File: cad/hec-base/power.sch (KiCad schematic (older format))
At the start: 45 parts

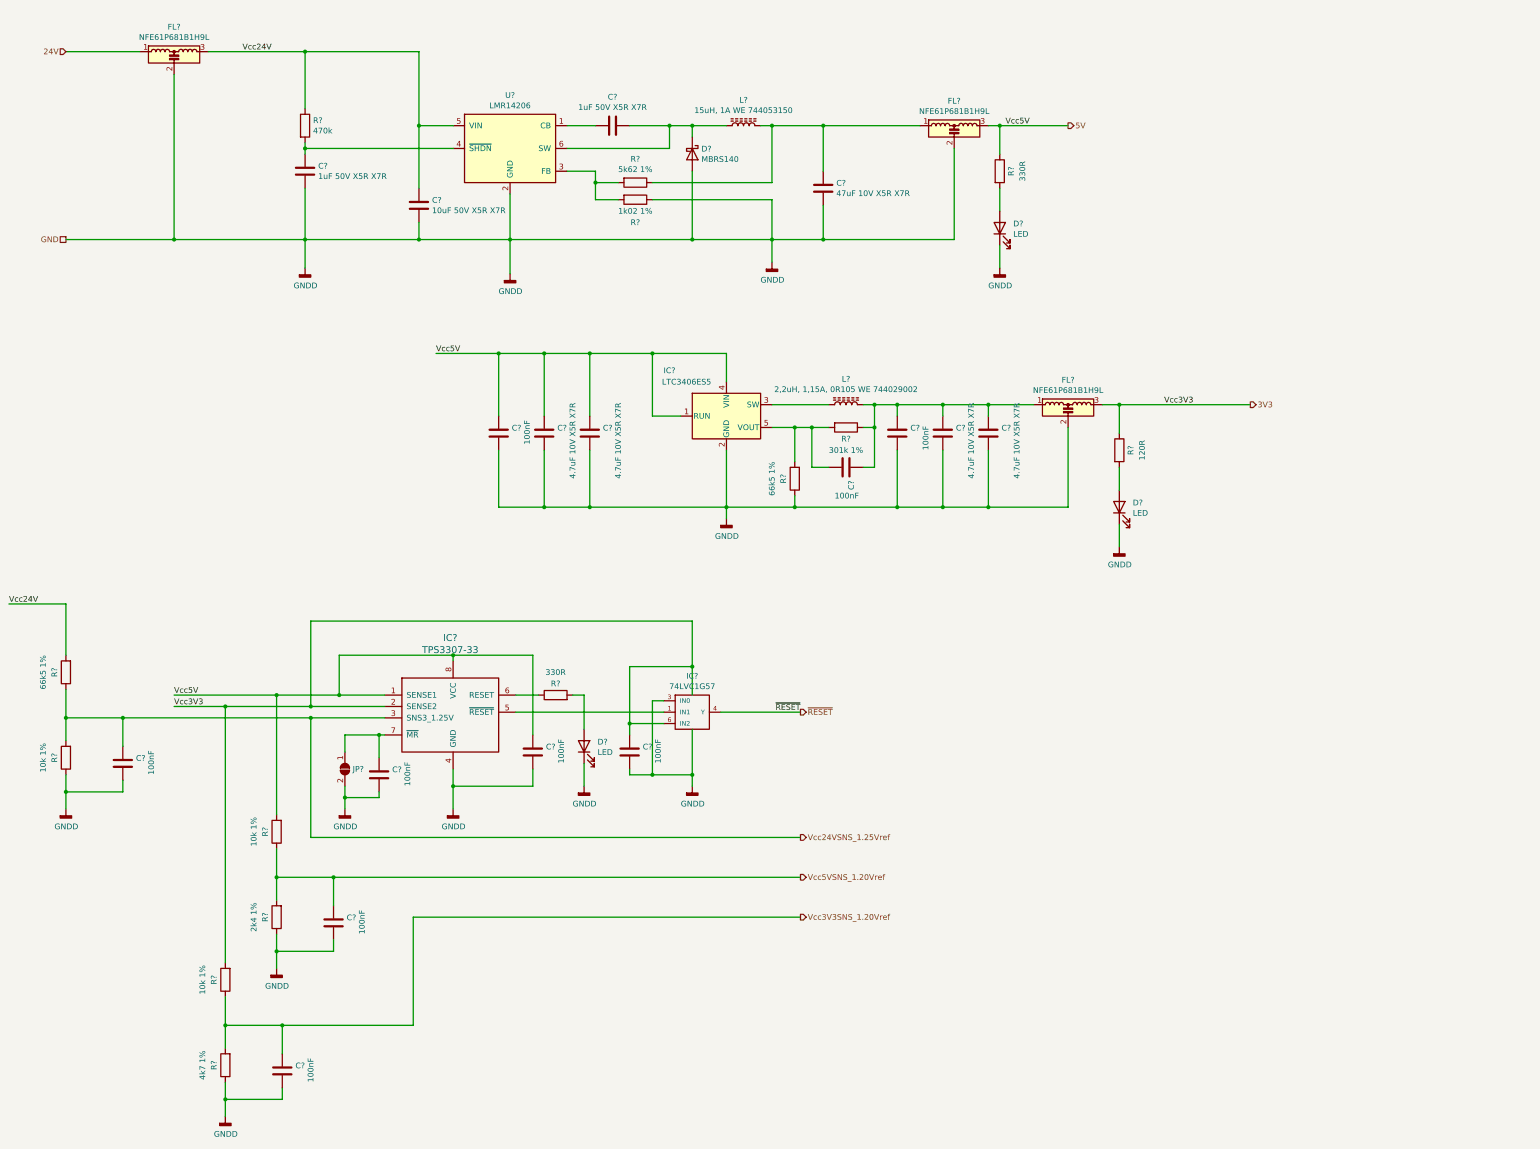
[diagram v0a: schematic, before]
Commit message: MCU-, Crypto- und One-Wire-Teil erstellt und dimensioniert, ERC bestanden, SLP geplottet, Footprints nur teilweise zugewiesen.
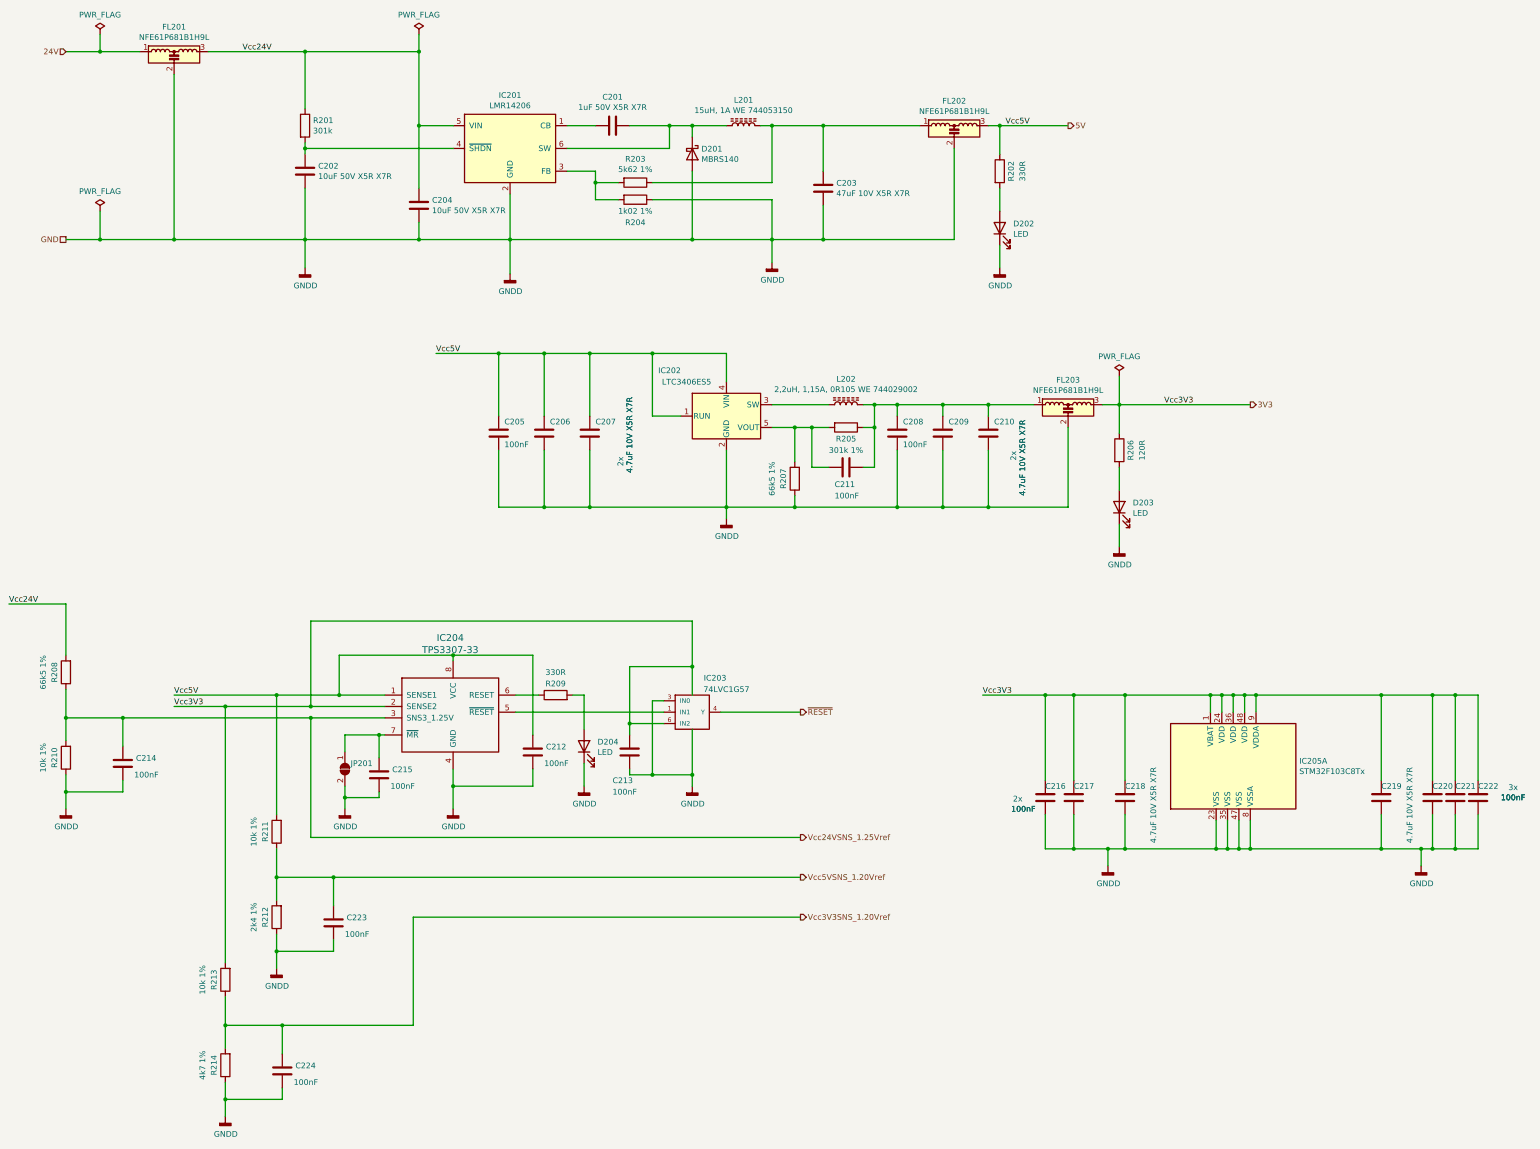
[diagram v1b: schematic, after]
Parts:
- added C216, C217, C220, C221, C222: 100nF, Capacitor_SMD:C_0603_1608Metric, symbol Device:C
- added C218, C219: 4.7uF 10V X5R X7R, Capacitor_SMD:C_0805_2012Metric, symbol Device:C
- added IC205: STM32F103C8Tx, Package_QFP:LQFP-48_7x7mm_P0.5mm, symbol MT_MCU_ST_STM32F1:STM32F103C8Tx
- C201, C206, C207, C209, C210: renamed from C?; footprint (none) -> Capacitor_SMD:C_0805_2012Metric
- C202: renamed from C?; value 1uF 50V X5R X7R -> 10uF 50V X5R X7R; footprint (none) -> Capacitor_SMD:C_1206_3216Metric
- C203: renamed from C?; footprint (none) -> Capacitor_SMD:C_1210_3225Metric
- C204: renamed from C?; footprint (none) -> Capacitor_SMD:C_1206_3216Metric
- C205, C208, C211, C212, C213, C214, C215, C223, C224: renamed from C?; footprint (none) -> Capacitor_SMD:C_0603_1608Metric
- D202, D203, D204: renamed from D?; footprint (none) -> LED_SMD:LED_0603_1608Metric
- IC203: renamed from IC?; footprint (none) -> Package_TO_SOT_SMD:SOT-363_SC-70-6
- IC204: renamed from IC?; footprint (none) -> Package_SO:SO-8_3.9x4.9mm_P1.27mm
- JP201: renamed from JP?; footprint (none) -> Jumper:SolderJumper-2_P1.3mm_Open_RoundedPad1.0x1.5mm
- L201: renamed from L?; footprint (none) -> Inductor_SMD:L_Wuerth_WE-TPC-3816
- R201: renamed from R?; value 470k -> 301k
- gave numbers to parts that had none: 20
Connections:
- net GND: now also C216.1, C217.1, C218.1, C219.1, C220.1, C221.1, C222.1, IC205.23 (VSS), IC205.35 (VSS), IC205.47 (VSS), IC205.8 (VSSA)
- net VCC: now also C216.2, C217.2, C218.2, C219.2, C220.2, C221.2, C222.2, IC205.1 (VBAT), IC205.24 (VDD), IC205.36 (VDD), IC205.48 (VDD), IC205.9 (VDDA)
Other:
- note added: "2x"
- note added: "3x"

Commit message: MT-Marienkaefer: Footprints fertig zugewiesen.
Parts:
- FL201, FL202, FL203: footprint (none) -> Filter_MT:Murata_NFE61P
- L202: footprint (none) -> Inductor_SMD:L_Wuerth_WE-TPC-3816
- R201, R202, R203, R204, R205, R206, R207, R208, R209, R210, R211, R212, R213, R214: footprint (none) -> Resistor_SMD:R_0603_1608Metric
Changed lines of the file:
@@
 F 0 "R201" H 4270 1696 50  0000 L CNN
 F 1 "301k" H 4270 1605 50  0000 L CNN
-F 2 "" V 4130 1650 50  0001 C CNN
+F 2 "Resistor_SMD:R_0603_1608Metric" V 4130 1650 50  0001 C CNN
 F 3 "~" H 4200 1650 50  0001 C CNN
 	1    4200 1650
@@
 F 0 "R204" V 7300 2300 50  0000 C CNN
 F 1 "1k02 1%" V 7200 2300 50  0000 C CNN
-F 2 "" V 7030 2300 50  0001 C CNN
+F 2 "Resistor_SMD:R_0603_1608Metric" V 7030 2300 50  0001 C CNN
 F 3 "~" H 7100 2300 50  0001 C CNN
 	1    7100 2300
@@
 F 0 "R203" V 6893 2150 50  0000 C CNN
 F 1 "5k62 1%" V 6984 2150 50  0000 C CNN
-F 2 "" V 7030 2150 50  0001 C CNN
+F 2 "Resistor_SMD:R_0603_1608Metric" V 7030 2150 50  0001 C CNN
 F 3 "~" H 7100 2150 50  0001 C CNN
 	1    7100 2150
@@
 F 0 "FL202" H 9900 2067 50  0000 C CNN
 F 1 "NFE61P681B1H9L" H 9900 1976 50  0000 C CNN
-F 2 "" V 9900 1750 50  0001 C CNN
+F 2 "Filter_MT:Murata_NFE61P" V 9900 1750 50  0001 C CNN
 F 3 "http://www.murata.com/~/media/webrenewal/support/library/catalog/products/emc/emifil/c31e.ashx?la=en-gb" V 9900 1750 50  0001 C CNN
 	1    9900 1750
@@
 F 0 "FL203" H 10900 4517 50  0000 C CNN
 F 1 "NFE61P681B1H9L" H 10900 4426 50  0000 C CNN
-F 2 "" V 10900 4200 50  0001 C CNN
+F 2 "Filter_MT:Murata_NFE61P" V 10900 4200 50  0001 C CNN
 F 3 "http://www.murata.com/~/media/webrenewal/support/library/catalog/products/emc/emifil/c31e.ashx?la=en-gb" V 10900 4200 50  0001 C CNN
 	1    10900 4200
@@
 F 0 "FL201" H 3050 1417 50  0000 C CNN
 F 1 "NFE61P681B1H9L" H 3050 1326 50  0000 C CNN
-F 2 "" V 3050 1100 50  0001 C CNN
+F 2 "Filter_MT:Murata_NFE61P" V 3050 1100 50  0001 C CNN
 F 3 "http://www.murata.com/~/media/webrenewal/support/library/catalog/products/emc/emifil/c31e.ashx?la=en-gb" V 3050 1100 50  0001 C CNN
 	1    3050 1100
@@
 F 0 "L202" V 9175 4100 50  0000 C CNN
 F 1 "2,2uH, 1,15A, 0R105 WE 744029002" V 9084 4100 50  0000 C CNN
-F 2 "" H 8950 4100 50  0001 C CNN
+F 2 "Inductor_SMD:L_Wuerth_WE-TPC-3816" H 8950 4100 50  0001 C CNN
 F 3 "~" H 8950 4100 50  0001 C CNN
 	1    8950 4100
@@
 F 0 "R205" V 9050 4300 50  0000 C CNN
 F 1 "301k 1%" V 9150 4300 50  0000 C CNN
-F 2 "" V 8880 4300 50  0001 C CNN
+F 2 "Resistor_SMD:R_0603_1608Metric" V 8880 4300 50  0001 C CNN
 F 3 "~" H 8950 4300 50  0001 C CNN
 	1    8950 4300
@@
 F 0 "R207" V 8600 4750 50  0000 C CNN
 F 1 "66k5 1%" V 8700 4750 50  0000 C CNN
-F 2 "" V 8430 4750 50  0001 C CNN
+F 2 "Resistor_SMD:R_0603_1608Metric" V 8430 4750 50  0001 C CNN
 F 3 "~" H 8500 4750 50  0001 C CNN
 	1    8500 4750
@@
 F 0 "R208" V 2200 6450 50  0000 C CNN
 F 1 "66k5 1%" V 2300 6450 50  0000 C CNN
-F 2 "" V 2030 6450 50  0001 C CNN
+F 2 "Resistor_SMD:R_0603_1608Metric" V 2030 6450 50  0001 C CNN
 F 3 "~" H 2100 6450 50  0001 C CNN
 	1    2100 6450
@@
 F 0 "R210" V 2200 7200 50  0000 C CNN
 F 1 "10k 1%" V 2300 7200 50  0000 C CNN
-F 2 "" V 2030 7200 50  0001 C CNN
+F 2 "Resistor_SMD:R_0603_1608Metric" V 2030 7200 50  0001 C CNN
 F 3 "~" H 2100 7200 50  0001 C CNN
 	1    2100 7200
@@
 F 0 "R209" V 6500 6650 50  0000 C CNN
 F 1 "330R" V 6600 6650 50  0000 C CNN
-F 2 "" V 6330 6650 50  0001 C CNN
+F 2 "Resistor_SMD:R_0603_1608Metric" V 6330 6650 50  0001 C CNN
 F 3 "~" H 6400 6650 50  0001 C CNN
 	1    6400 6650
@@
 F 0 "R202" V 10400 2050 50  0000 C CNN
 F 1 "330R" V 10500 2050 50  0000 C CNN
-F 2 "" V 10230 2050 50  0001 C CNN
+F 2 "Resistor_SMD:R_0603_1608Metric" V 10230 2050 50  0001 C CNN
 F 3 "~" H 10300 2050 50  0001 C CNN
 	1    10300 2050
@@
 F 0 "R206" V 11450 4500 50  0000 C CNN
 F 1 "120R" V 11550 4500 50  0000 C CNN
-F 2 "" V 11280 4500 50  0001 C CNN
+F 2 "Resistor_SMD:R_0603_1608Metric" V 11280 4500 50  0001 C CNN
 F 3 "~" H 11350 4500 50  0001 C CNN
 	1    11350 4500
@@
 F 0 "R211" V 4050 7850 50  0000 C CNN
 F 1 "10k 1%" V 4150 7850 50  0000 C CNN
-F 2 "" V 3880 7850 50  0001 C CNN
+F 2 "Resistor_SMD:R_0603_1608Metric" V 3880 7850 50  0001 C CNN
 F 3 "~" H 3950 7850 50  0001 C CNN
 	1    3950 7850
@@
 F 0 "R212" V 4050 8600 50  0000 C CNN
 F 1 "2k4 1%" V 4150 8600 50  0000 C CNN
-F 2 "" V 3880 8600 50  0001 C CNN
+F 2 "Resistor_SMD:R_0603_1608Metric" V 3880 8600 50  0001 C CNN
 F 3 "~" H 3950 8600 50  0001 C CNN
 	1    3950 8600
@@
 F 0 "R213" V 3600 9150 50  0000 C CNN
 F 1 "10k 1%" V 3700 9150 50  0000 C CNN
-F 2 "" V 3430 9150 50  0001 C CNN
+F 2 "Resistor_SMD:R_0603_1608Metric" V 3430 9150 50  0001 C CNN
 F 3 "~" H 3500 9150 50  0001 C CNN
 	1    3500 9150
@@
 F 0 "R214" V 3600 9900 50  0000 C CNN
 F 1 "4k7 1%" V 3700 9900 50  0000 C CNN
-F 2 "" V 3430 9900 50  0001 C CNN
+F 2 "Resistor_SMD:R_0603_1608Metric" V 3430 9900 50  0001 C CNN
 F 3 "~" H 3500 9900 50  0001 C CNN
 	1    3500 9900

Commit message: Entflochtene Leiterplatte mit Schaltplan speichern.
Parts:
- added unit 2 of IC203
- added R215: 120R, Resistor_SMD:R_0603_1608Metric, symbol Device:R
- FL201, FL202, FL203: symbol Device:EMI_Filter_LCL -> Device:Filter_EMI_LCL
- IC203: symbol 74xGxx:74AUP1G57 -> Logic_74xGxx_MT:74LVC1G57
- L201: symbol Device:L_Core_Ferrite -> Device:L_Ferrite
- L202: value 2,2uH, 1,15A, 0R105 WE 744029002 -> 2,5uH, 1,25A, 0R05 WE 744031002; symbol Device:L_Core_Ferrite -> Device:L_Ferrite
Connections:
- net ~RESET~: now also R215.2; no longer IC203.4 (Y)
- net GND renamed GNDD
- net GNDD: now also IC203.2 (GND); no longer IC203.2 (GND)
- net VCC renamed 3V3
- net 3V3: now also IC203.5 (VCC); no longer IC203.5 (VCC)
- new net: IC203.4 (Y), R215.1
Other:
- note added: "Levelshifter 5V domain into 3V3 domain\n(2-Input NAND,with ~A~, B tied up)"
- moved on the sheet: C213, IC203A
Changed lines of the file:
@@
 encoding utf-8
 Sheet 2 5
-Title "Marienkäfer HEC-Basis-Bord: Stromversorgung"
+Title "Marienkaefer HEC-Basis-Bord: Stromversorgung"
 Date "2020-12-29"
 Rev "0001"
@@
 $EndComp
 $Comp
-L Device:L_Core_Ferrite L201
+L Device:L_Ferrite L201
 U 1 1 601394EC
 P 8050 1650
@@
 $EndComp
 $Comp
-L Device:EMI_Filter_LCL FL202
+L Device:Filter_EMI_LCL FL202
 U 1 1 6014A133
 P 9900 1750
@@
 	10900 1650 10300 1650
 $Comp
-L Device:EMI_Filter_LCL FL203
+L Device:Filter_EMI_LCL FL203
 U 1 1 6015060B
 P 10900 4200
@@
 $EndComp
 $Comp
-L Device:EMI_Filter_LCL FL201
+L Device:Filter_EMI_LCL FL201
 U 1 1 60151B34
 P 3050 1100
@@
 	3050 2650 4200 2650
 $Comp
-L Device:L_Core_Ferrite L202
+L Device:L_Ferrite L202
 U 1 1 60157375
 P 8950 4100
 F 0 "L202" V 9175 4100 50  0000 C CNN
-F 1 "2,2uH, 1,15A, 0R105 WE 744029002" V 9084 4100 50  0000 C CNN
+F 1 "2,5uH, 1,25A, 0R05 WE 744031002" V 9084 4100 50  0000 C CNN
 F 2 "Inductor_SMD:L_Wuerth_WE-TPC-3816" H 8950 4100 50  0001 C CNN
 F 3 "~" H 8950 4100 50  0001 C CNN
@@
 	4500 6650 3950 6650
 $Comp
-L 74xGxx:74AUP1G57 IC203
-U 1 1 60212CEA
-P 7600 6800
-F 0 "IC203" H 7800 7100 50  0000 C CNN
-F 1 "74LVC1G57" H 7900 7000 50  0000 C CNN
-F 2 "Package_TO_SOT_SMD:SOT-363_SC-70-6" H 7600 6800 50  0001 C CNN
-F 3 "http://www.ti.com/lit/sg/scyt129e/scyt129e.pdf" H 7600 6800 50  0001 C CNN
-	1    7600 6800
-	1    0    0    -1
-$EndComp
-$Comp
 L power:GNDD #PWR0208
 U 1 1 60212F05
-P 7600 7450
-F 0 "#PWR0208" H 7600 7200 50  0001 C CNN
-F 1 "GNDD" H 7604 7295 50  0000 C CNN
-F 2 "" H 7600 7450 50  0001 C CNN
-F 3 "" H 7600 7450 50  0001 C CNN
-	1    7600 7450
+P 7400 7000
+F 0 "#PWR0208" H 7400 6750 50  0001 C CNN
+F 1 "GNDD" H 7404 6845 50  0000 C CNN
+F 2 "" H 7400 7000 50  0001 C CNN
+F 3 "" H 7400 7000 50  0001 C CNN
+	1    7400 7000
 	1    0    0    -1
 $EndComp
@@
 L Device:C C213
 U 1 1 602132EE
-P 7050 7150
-F 0 "C213" H 7200 7400 50  0000 R CNN
-F 1 "100nF" H 7200 7500 50  0000 R CNN
-F 2 "Capacitor_SMD:C_0603_1608Metric" H 7088 7000 50  0001 C CNN
-F 3 "~" H 7050 7150 50  0001 C CNN
-	1    7050 7150
-	-1   0    0    1
-$EndComp
-Wire Wire Line
-	4250 6750 4250 6000
-Wire Wire Line
-	4250 6000 7600 6000
-Wire Wire Line
-	7600 6000 7600 6400
-Connection ~ 4250 6750
-Wire Wire Line
-	4250 6750 4900 6750
-Wire Wire Line
-	7600 6950 7600 7350
-Wire Wire Line
-	7050 7300 7050 7350
-Wire Wire Line
-	7050 7350 7250 7350
-Connection ~ 7600 7350
-Wire Wire Line
-	7600 7350 7600 7450
-Wire Wire Line
-	7600 6400 7050 6400
-Wire Wire Line
-	7050 6400 7050 6900
-Connection ~ 7600 6400
-Wire Wire Line
-	7600 6400 7600 6650
-Wire Wire Line
-	7850 6800 8550 6800
-Wire Wire Line
-	7350 6800 6050 6800
-Wire Wire Line
-	7350 6700 7250 6700
-Wire Wire Line
-	7250 6700 7250 7350
-Connection ~ 7250 7350
-Wire Wire Line
-	7250 7350 7600 7350
-Wire Wire Line
-	7350 6900 7050 6900
-Connection ~ 7050 6900
-Wire Wire Line
-	7050 6900 7050 7000
+P 9800 7150
+F 0 "C213" H 9914 7104 50  0000 L CNN
+F 1 "100nF" H 9914 7195 50  0000 L CNN
+F 2 "Capacitor_SMD:C_0603_1608Metric" H 9838 7000 50  0001 C CNN
+F 3 "~" H 9800 7150 50  0001 C CNN
+	1    9800 7150
+	-1   0    0    1
+$EndComp
+Wire Wire Line
+	8000 6800 8200 6800
+Wire Wire Line
+	7500 6800 6050 6800
+Wire Wire Line
+	7500 6700 7400 6700
 $Comp
 L Device:LED D204
@@
 Wire Wire Line
 	4250 6850 2600 6850
-Text HLabel 8550 6800 2    50   Output ~ 0
+Text HLabel 8750 6800 2    50   Output ~ 0
 ~RESET~
 Text HLabel 8550 7900 2    50   Output ~ 0
@@
 Connection ~ 3500 6750
 Wire Wire Line
-	3500 6750 4250 6750
-Wire Wire Line
 	5150 9550 5150 8600
 Wire Wire Line
@@
 	10950 6650 11400 6650
 Wire Wire Line
-	10700 6650 10150 6650
+	10700 6650 10250 6650
 Connection ~ 10700 6650
-Text Label 10150 6650 0    50   ~ 0
+Text Label 9400 6650 0    50   ~ 0
 Vcc3V3
 Text Notes 10450 4600 1    50   ~ 0
@@
 	-1   0    0    1
 $EndComp
+Wire Wire Line
+	7050 6350 7050 6900
+$Comp
+L Logic_74xGxx_MT:74LVC1G57 IC203
+U 1 1 60212CEA
+P 7600 6950
+F 0 "IC203" H 7750 7417 50  0000 C CNN
+F 1 "74LVC1G57" H 7750 7326 50  0000 C CNN
+F 2 "Package_TO_SOT_SMD:SOT-363_SC-70-6" H 7600 6950 50  0001 C CNN
+F 3 "http://www.ti.com/lit/sg/scyt129e/scyt129e.pdf" H 7600 6950 50  0001 C CNN
+	1    7600 6950
+	1    0    0    -1
+$EndComp
+$Comp
+L Logic_74xGxx_MT:74LVC1G57 IC203
+U 2 1 63330CB8
+P 10100 7200
+F 0 "IC203" H 10100 7150 50  0000 L CNN
+F 1 "74LVC1G57" H 10100 7050 50  0000 L CNN
+F 2 "Package_TO_SOT_SMD:SOT-363_SC-70-6" H 10100 7200 50  0001 C CNN
+F 3 "http://www.ti.com/lit/sg/scyt129e/scyt129e.pdf" H 10100 7200 50  0001 C CNN
+	2    10100 7200
+	1    0    0    -1
+$EndComp
+$Comp
+L power:PWR_FLAG #FLG0105
+U 1 1 633B9556
+P 10300 1450
+F 0 "#FLG0105" H 10300 1525 50  0001 C CNN
+F 1 "PWR_FLAG" H 10300 1623 50  0000 C CNN
+F 2 "" H 10300 1450 50  0001 C CNN
+F 3 "~" H 10300 1450 50  0001 C CNN
+	1    10300 1450
+	1    0    0    -1
+$EndComp
+Wire Wire Line
+	10300 1450 10300 1650
+Wire Wire Line
+	10250 6800 10250 6650
+Connection ~ 10250 6650
+Wire Wire Line
+	10250 6650 9800 6650
+Wire Wire Line
+	10700 8000 10050 8000
+Wire Wire Line
+	10050 8000 10050 7300
+Connection ~ 10700 8000
+Wire Wire Line
+	7050 6900 7500 6900
+Wire Wire Line
+	9800 7000 9800 6650
+Connection ~ 9800 6650
+Wire Wire Line
+	9800 6650 9400 6650
+Wire Wire Line
+	9800 7300 9800 8000
+Wire Wire Line
+	9800 8000 10050 8000
+Connection ~ 10050 8000
+Wire Wire Line
+	7400 6700 7400 7000
+Wire Wire Line
+	3500 6750 4900 6750
+Wire Wire Line
+	7050 6350 8200 6350
+Text Label 8200 6350 2    50   ~ 0
+Vcc3V3
+Text Notes 7150 7400 0    50   ~ 0
+Levelshifter 5V domain into 3V3 domain\n(2-Input NAND,with ~A~, B tied up)
+$Comp
+L Device:R R215
+U 1 1 6318A2F0
+P 8350 6800
+F 0 "R215" V 8450 6800 50  0000 C CNN
+F 1 "120R" V 8550 6800 50  0000 C CNN
+F 2 "Resistor_SMD:R_0603_1608Metric" V 8280 6800 50  0001 C CNN
+F 3 "~" H 8350 6800 50  0001 C CNN
+	1    8350 6800
+	0    -1   -1   0
+$EndComp
+Wire Wire Line
+	8500 6800 8750 6800
 $EndSCHEMATC
